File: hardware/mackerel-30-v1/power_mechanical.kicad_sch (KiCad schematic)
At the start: 21 parts, among them J10 Conn_02x03_Odd_Even, J7 Barrel_Jack_MountingPin, J8 Conn_02x03_Odd_Even, J9 Conn_02x03_Odd_Even, U7 AMS1117-3.3, U8 LM2576T-5

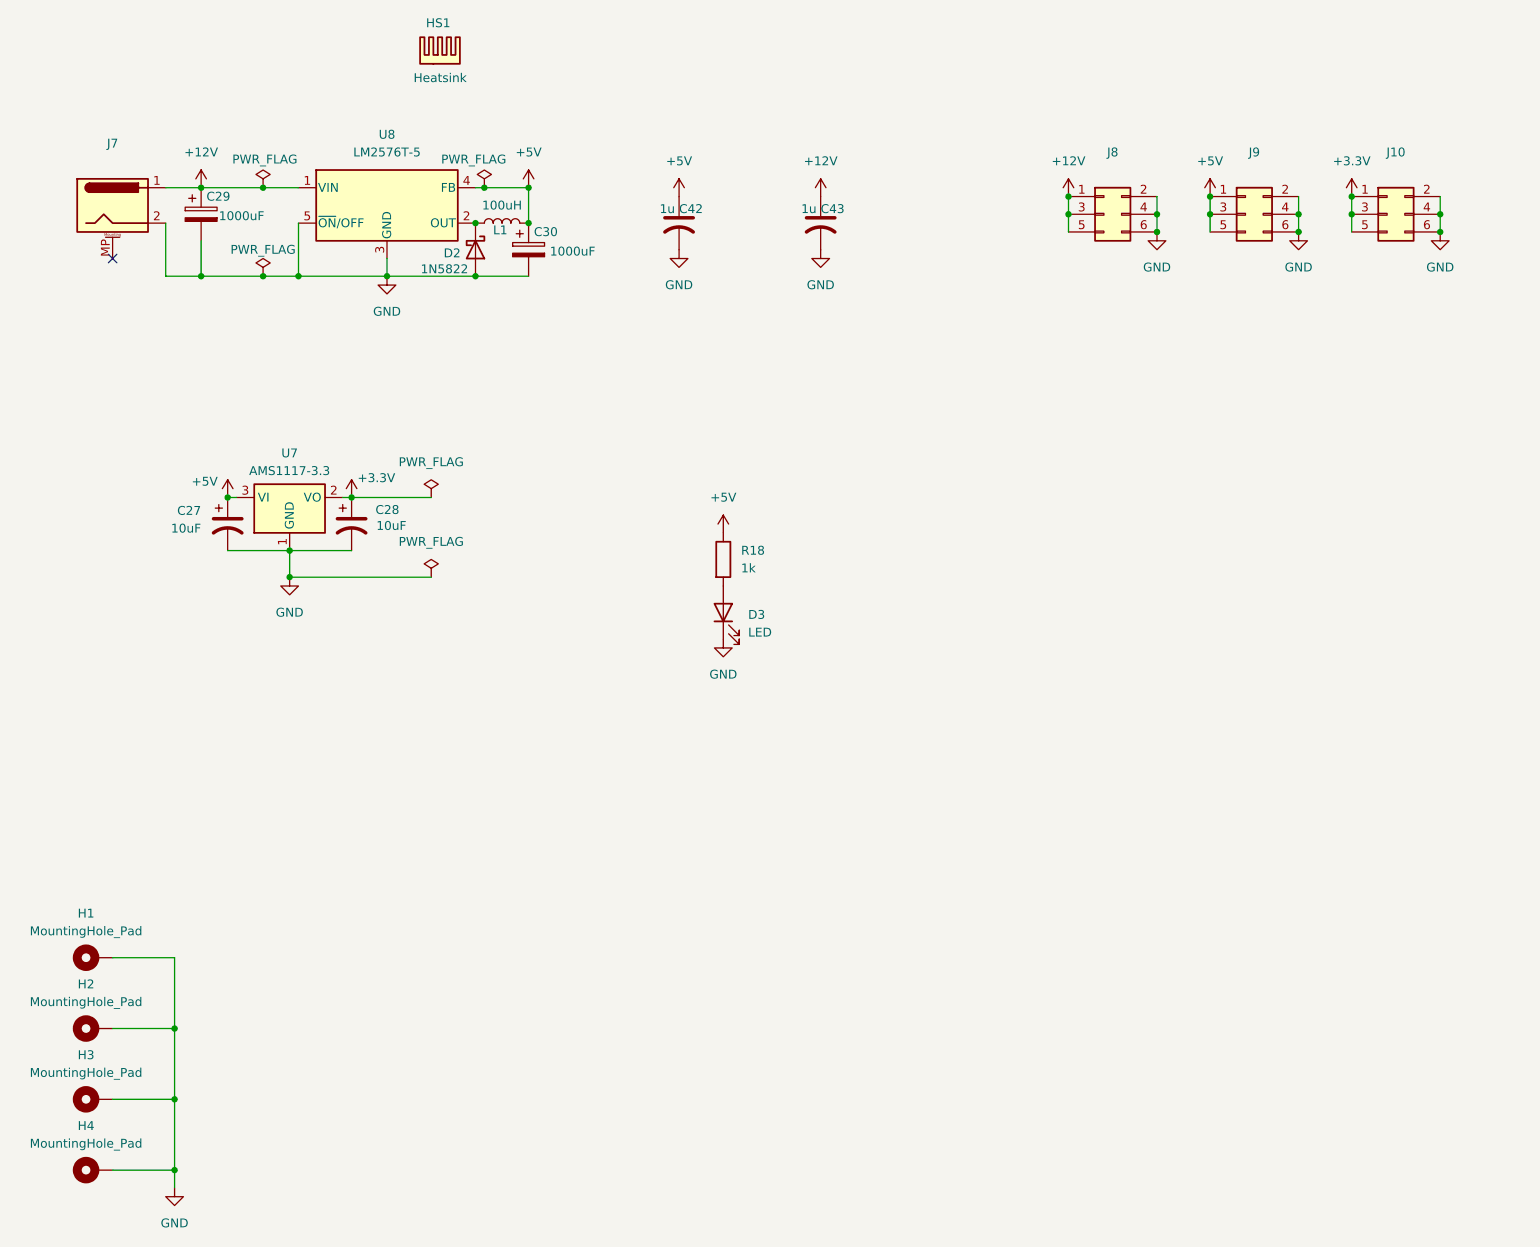
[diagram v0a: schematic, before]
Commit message: SIMM and data buffers mostly routed
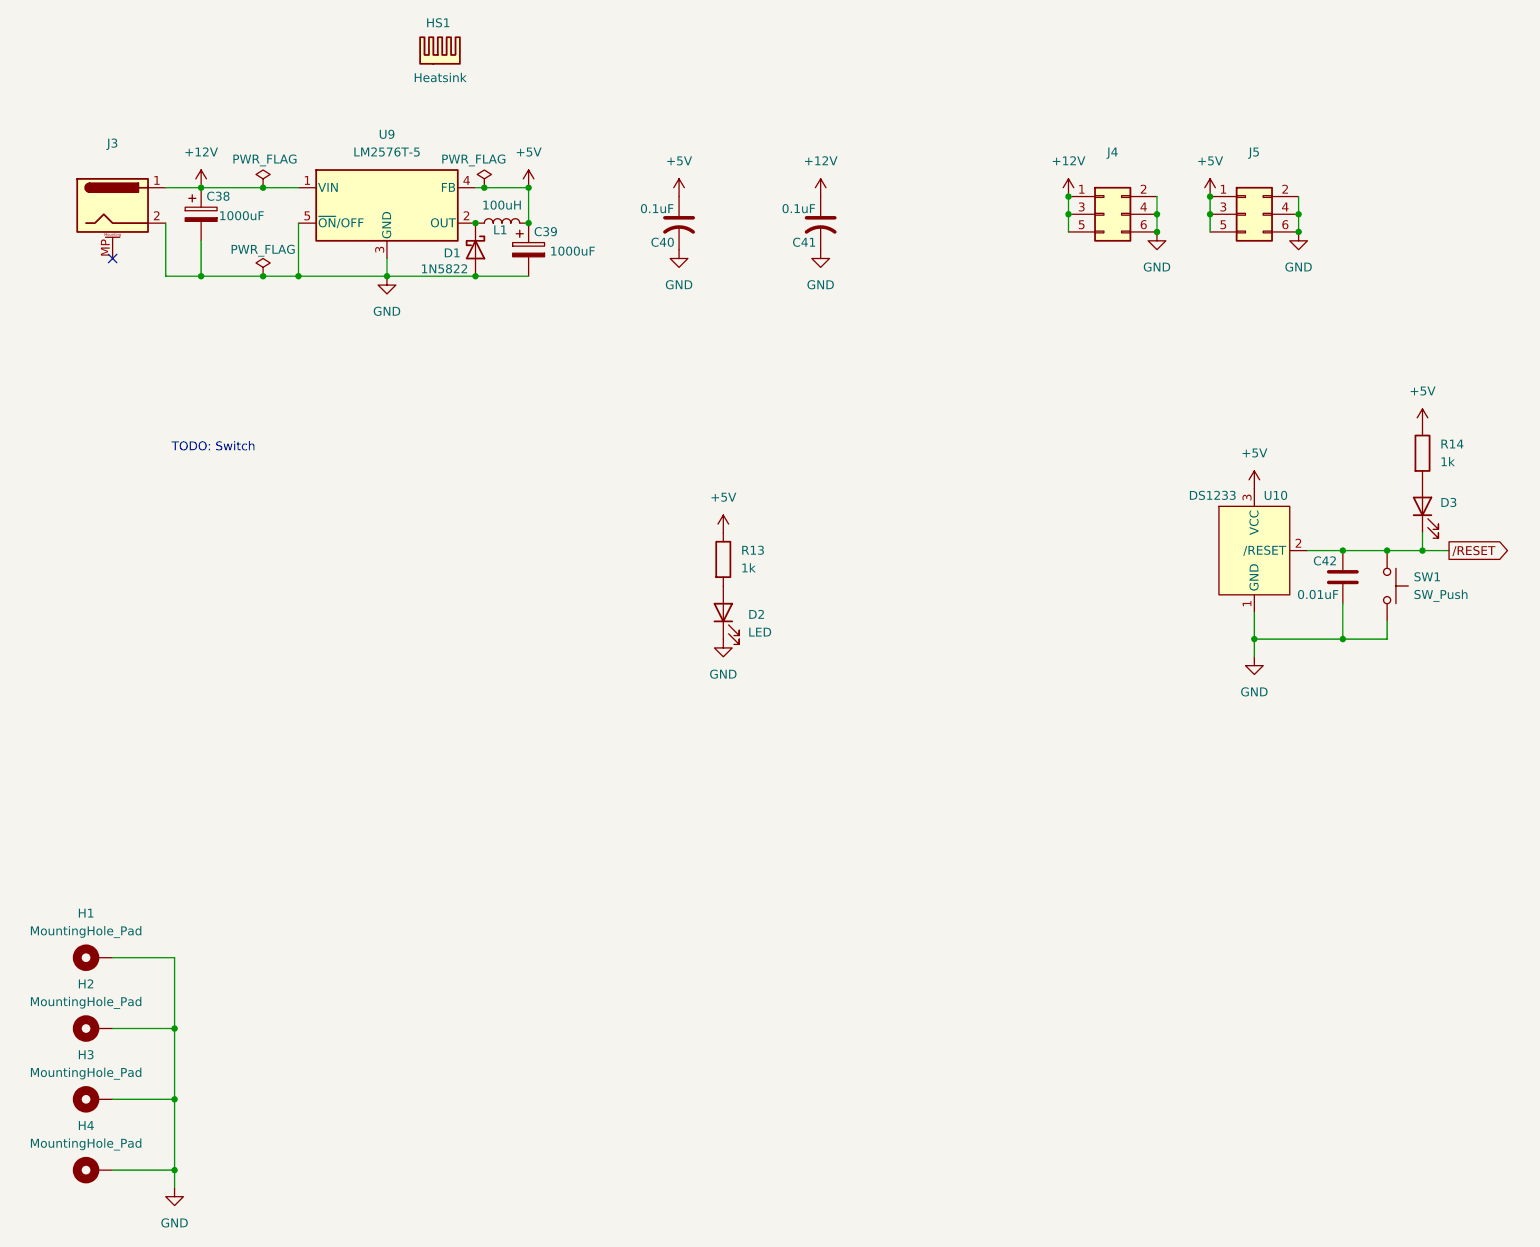
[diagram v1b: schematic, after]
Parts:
- removed C27, C28: 10uF, Capacitor_THT:CP_Radial_D5.0mm_P2.00mm, symbol Device:C_Polarized_US
- removed J10: Conn_02x03_Odd_Even, Connector_PinHeader_2.54mm:PinHeader_2x03_P2.54mm_Vertical, symbol Connector_Generic:Conn_02x03_Odd_Even
- removed U7: AMS1117-3.3, Package_TO_SOT_SMD:SOT-223-3_TabPin2, symbol Regulator_Linear:AMS1117-3.3
- added C42: 0.01uF, Capacitor_SMD:C_1206_3216Metric_Pad1.33x1.80mm_HandSolder, symbol Device:C
- added D3: LED, LED_THT:LED_D5.0mm, symbol Device:LED
- added R14: 1k, Resistor_SMD:R_1206_3216Metric_Pad1.30x1.75mm_HandSolder, symbol Device:R
- added SW1: SW_Push, Button_Switch_THT:SW_PUSH_6mm_H5mm, symbol Switch:SW_Push
- added U10: DS1233, Package_TO_SOT_THT:TO-92L_Wide, symbol mackerel-68k-symbols:DS1233
- C40: renamed from C42; value 1u -> 0.1uF; footprint Capacitor_SMD:C_0805_2012Metric_Pad1.18x1.45mm_HandSolder -> Capacitor_SMD:C_1206_3216Metric_Pad1.33x1.80mm_HandSolder
- C41: renamed from C43; value 1u -> 0.1uF; footprint Capacitor_SMD:C_0805_2012Metric_Pad1.18x1.45mm_HandSolder -> Capacitor_SMD:C_1206_3216Metric_Pad1.33x1.80mm_HandSolder
- R13: renamed from R18; footprint Resistor_THT:R_Axial_DIN0207_L6.3mm_D2.5mm_P7.62mm_Horizontal -> Resistor_SMD:R_1206_3216Metric_Pad1.30x1.75mm_HandSolder
- renumbered C29 to C38, C30 to C39, D2 to D1, D3 to D2, J7 to J3, J8 to J4, J9 to J5, U8 to U9
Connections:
- net +5V: now also R14.1, U10.3 (VCC)
- net GND: now also C42.2, SW1.2, U10.1 (GND)
- new net: D3.2 (A), R14.2
- new net /RESET: C42.1, D3.1 (K), SW1.1, U10.2 (/RESET)
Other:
- note added: "TODO: Switch"
